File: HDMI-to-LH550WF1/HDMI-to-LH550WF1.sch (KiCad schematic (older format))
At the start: 2 parts

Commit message: Annotated schematic and associated footprints
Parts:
- P1: renamed from P?; footprint (none) -> Connect:USB_Mini-B
- P2: renamed from P?; footprint (none) -> connectors:FCI_10029449-111RLF
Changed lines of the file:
@@
 $EndSheet
 $Comp
-L USB_OTG P?
+L USB_OTG P1
 U 1 1 583A5572
 P 2300 4500
-F 0 "P?" H 2625 4375 50  0000 C CNN
+F 0 "P1" H 2625 4375 50  0000 C CNN
 F 1 "USB_OTG" H 2300 4700 50  0000 C CNN
-F 2 "" V 2250 4400 50  0000 C CNN
+F 2 "Connect:USB_Mini-B" V 2250 4400 50  0001 C CNN
 F 3 "" V 2250 4400 50  0000 C CNN
 	1    2300 4500
@@
 NoConn ~ 2600 4400
 $Comp
-L GND #PWR?
+L GND #PWR01
 U 1 1 583A6AC9
 P 1900 4200
-F 0 "#PWR?" H 1900 3950 50  0001 C CNN
+F 0 "#PWR01" H 1900 3950 50  0001 C CNN
 F 1 "GND" H 1900 4050 50  0000 C CNN
 F 2 "" H 1900 4200 50  0000 C CNN
@@
 	3100 4700 2600 4700
 $Comp
-L GND #PWR?
+L GND #PWR02
 U 1 1 58414197
 P 3300 1400
-F 0 "#PWR?" H 3300 1150 50  0001 C CNN
+F 0 "#PWR02" H 3300 1150 50  0001 C CNN
 F 1 "GND" H 3300 1250 50  0000 C CNN
 F 2 "" H 3300 1400 50  0000 C CNN
@@
 HPD
 $Comp
-L GND #PWR?
+L GND #PWR03
 U 1 1 5841821A
 P 3600 1700
-F 0 "#PWR?" H 3600 1450 50  0001 C CNN
+F 0 "#PWR03" H 3600 1450 50  0001 C CNN
 F 1 "GND" H 3600 1550 50  0000 C CNN
 F 2 "" H 3600 1700 50  0000 C CNN
@@
 $EndComp
 $Comp
-L GND #PWR?
+L GND #PWR04
 U 1 1 5841833B
 P 3600 2000
-F 0 "#PWR?" H 3600 1750 50  0001 C CNN
+F 0 "#PWR04" H 3600 1750 50  0001 C CNN
 F 1 "GND" H 3600 1850 50  0000 C CNN
 F 2 "" H 3600 2000 50  0000 C CNN
@@
 $EndComp
 $Comp
-L GND #PWR?
+L GND #PWR05
 U 1 1 5841845A
 P 3600 2300
-F 0 "#PWR?" H 3600 2050 50  0001 C CNN
+F 0 "#PWR05" H 3600 2050 50  0001 C CNN
 F 1 "GND" H 3600 2150 50  0000 C CNN
 F 2 "" H 3600 2300 50  0000 C CNN
@@
 $EndComp
 $Comp
-L GND #PWR?
+L GND #PWR06
 U 1 1 58418579
 P 3600 2600
-F 0 "#PWR?" H 3600 2350 50  0001 C CNN
+F 0 "#PWR06" H 3600 2350 50  0001 C CNN
 F 1 "GND" H 3600 2450 50  0000 C CNN
 F 2 "" H 3600 2600 50  0000 C CNN
@@
 $EndComp
 $Comp
-L GND #PWR?
+L GND #PWR07
 U 1 1 58418698
 P 3600 3200
-F 0 "#PWR?" H 3600 2950 50  0001 C CNN
+F 0 "#PWR07" H 3600 2950 50  0001 C CNN
 F 1 "GND" H 3600 3050 50  0000 C CNN
 F 2 "" H 3600 3200 50  0000 C CNN
@@
 CLKP
 $Comp
-L HDMI P?
+L HDMI P2
 U 1 1 584141D8
 P 2800 2400
-F 0 "P?" H 2600 3650 60  0000 L CNN
+F 0 "P2" H 2600 3650 60  0000 L CNN
 F 1 "HDMI" H 2600 1150 60  0000 L CNN
-F 2 "" H 2700 2300 60  0001 C CNN
+F 2 "connectors:FCI_10029449-111RLF" H 2700 2300 60  0001 C CNN
 F 3 "" H 2700 2300 60  0001 C CNN
 	1    2800 2400

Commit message: Renamed some nets to enable differential routing
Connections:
- net labels added: CLK_N, CLK_P, D0_N, D0_P, D1_N, D1_P, D2_N, D2_P
- net labels removed: CLKN, CLKP, D0N, D0P, D1N, D1P, D2N, D2P
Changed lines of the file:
@@
 F0 "LCD-Panel" 60
 F1 "LCD-Panel.sch" 60
-F2 "DATA3P" I L 8500 2900 60
-F3 "DATA3N" I L 8500 2800 60
-F4 "DATA2P" I L 8500 3100 60
-F5 "DATA2N" I L 8500 3000 60
-F6 "CLKP" I L 8500 3700 60
-F7 "CLKN" I L 8500 3600 60
-F8 "DATA1N" I L 8500 3200 60
-F9 "DATA1P" I L 8500 3300 60
-F10 "DATA0P" I L 8500 3500 60
-F11 "DATA0N" I L 8500 3400 60
+F2 "DATA3_P" I L 8500 2900 60
+F3 "DATA3_N" I L 8500 2800 60
+F4 "DATA2_P" I L 8500 3100 60
+F5 "DATA2_N" I L 8500 3000 60
+F6 "CLK_P" I L 8500 3700 60
+F7 "CLK_N" I L 8500 3600 60
+F8 "DATA1_N" I L 8500 3200 60
+F9 "DATA1_P" I L 8500 3300 60
+F10 "DATA0_P" I L 8500 3500 60
+F11 "DATA0_N" I L 8500 3400 60
 F12 "RESET" I L 8500 3900 60
 $EndSheet
@@
 	3200 1600 3600 1600
 Text Label 3600 1600 2    60   ~ 0
-D2P
+D2_P
 Text Label 3600 1800 2    60   ~ 0
-D2N
+D2_N
 Text Label 3600 1900 2    60   ~ 0
-D1P
+D1_P
 Text Label 3600 2100 2    60   ~ 0
-D1N
+D1_N
 Text Label 3600 2200 2    60   ~ 0
-D0P
+D0_P
 Text Label 3600 2400 2    60   ~ 0
-D0N
+D0_N
 Text Label 3600 2500 2    60   ~ 0
-CLKP
+CLK_P
 Text Label 3600 2700 2    60   ~ 0
-CLKN
+CLK_N
 Text Label 3600 3000 2    60   ~ 0
 SCL
@@
 SCL
 Text Label 5300 3500 0    60   ~ 0
-D2N
+D2_N
 Text Label 5300 3400 0    60   ~ 0
-D2P
+D2_P
 Text Label 5300 3300 0    60   ~ 0
-D1N
+D1_N
 Text Label 5300 3200 0    60   ~ 0
-D1P
+D1_P
 Text Label 5300 3100 0    60   ~ 0
-D0N
+D0_N
 Text Label 5300 3000 0    60   ~ 0
-D0P
+D0_P
 Text Label 5300 2900 0    60   ~ 0
-CLKN
+CLK_N
 Text Label 5300 2800 0    60   ~ 0
-CLKP
+CLK_P
 $Comp
 L HDMI P2

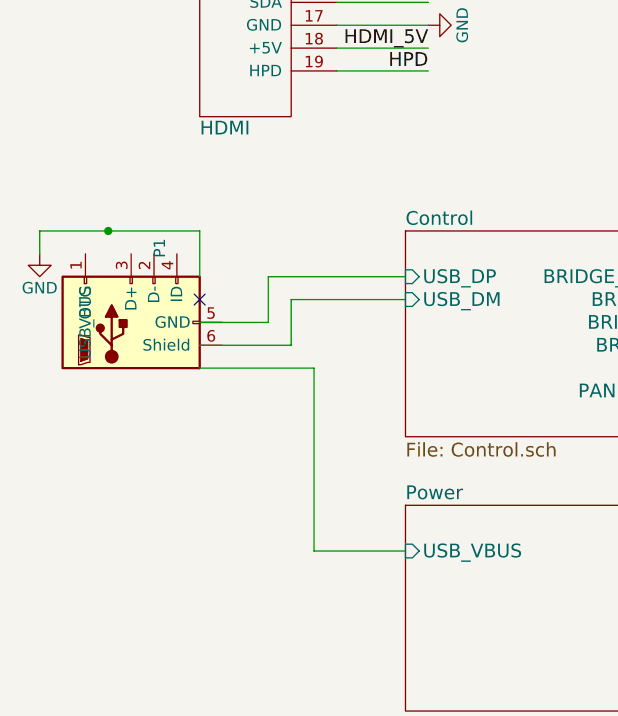
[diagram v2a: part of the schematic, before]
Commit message: Replace USB connector symbol with updated version
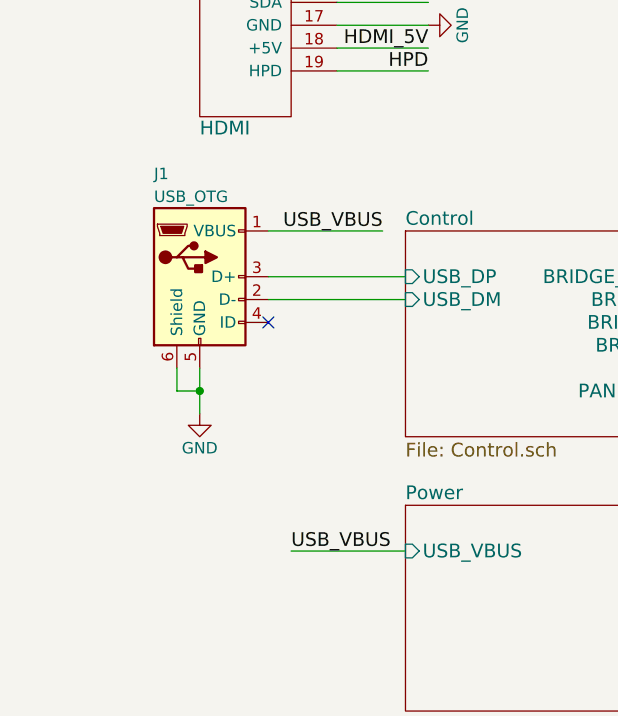
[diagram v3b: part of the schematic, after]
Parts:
- removed P1: USB_OTG, Connect:USB_Mini-B, symbol USB_OTG
- added J1: USB_OTG, Connect:USB_Micro-B, symbol USB_OTG
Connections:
- net labels added: USB_VBUS
- wire segments 67 -> 62
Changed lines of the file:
@@
 $EndSheet
-$Comp
-L USB_OTG P1
-U 1 1 583A5572
-P 2300 4500
-F 0 "P1" H 2625 4375 50  0000 C CNN
-F 1 "USB_OTG" H 2300 4700 50  0000 C CNN
-F 2 "Connect:USB_Mini-B" V 2250 4400 50  0001 C CNN
-F 3 "" V 2250 4400 50  0000 C CNN
-	1    2300 4500
-	0    -1   -1   0
-$EndComp
-NoConn ~ 2600 4400
 $Comp
 L GND #PWR01
 U 1 1 583A6AC9
-P 1900 4200
-F 0 "#PWR01" H 1900 3950 50  0001 C CNN
-F 1 "GND" H 1900 4050 50  0000 C CNN
-F 2 "" H 1900 4200 50  0000 C CNN
-F 3 "" H 1900 4200 50  0000 C CNN
-	1    1900 4200
+P 2600 4900
+F 0 "#PWR01" H 2600 4650 50  0001 C CNN
+F 1 "GND" H 2600 4750 50  0000 C CNN
+F 2 "" H 2600 4900 50  0000 C CNN
+F 3 "" H 2600 4900 50  0000 C CNN
+	1    2600 4900
 	1    0    0    -1
 $EndComp
@@
 	7300 3700 8500 3700
 Wire Wire Line
-	2600 4100 2600 4300
-Wire Wire Line
-	1900 4100 2600 4100
-Wire Wire Line
-	1900 4100 1900 4200
-Connection ~ 2200 4100
+	2600 4700 2600 4900
 Wire Wire Line
 	5200 4100 5200 4300
@@
 	7600 3900 8500 3900
 Wire Wire Line
-	2600 4500 2900 4500
-Wire Wire Line
-	2600 4600 3000 4600
-Wire Wire Line
 	5200 4300 4900 4300
 Wire Wire Line
@@
 	3500 4300 2900 4300
 Wire Wire Line
-	2900 4300 2900 4500
-Wire Wire Line
-	3500 4400 3000 4400
-Wire Wire Line
-	3000 4400 3000 4600
-Wire Wire Line
-	3500 5500 3100 5500
-Wire Wire Line
-	3100 5500 3100 4700
-Wire Wire Line
-	3100 4700 2600 4700
+	2900 4400 3500 4400
+Wire Wire Line
+	3000 5500 3500 5500
 $Comp
 L GND #PWR02
@@
 	1    0    0    -1
 $EndComp
+$Comp
+L USB_OTG J1
+U 1 1 58F8583B
+P 2600 4300
+F 0 "J1" H 2400 4750 50  0000 L CNN
+F 1 "USB_OTG" H 2400 4650 50  0000 L CNN
+F 2 "Connect:USB_Micro-B" H 2750 4250 50  0001 C CNN
+F 3 "" H 2750 4250 50  0001 C CNN
+	1    2600 4300
+	1    0    0    -1
+$EndComp
+Wire Wire Line
+	2500 4700 2500 4800
+Wire Wire Line
+	2500 4800 2600 4800
+Connection ~ 2600 4800
+Text Label 3400 4100 2    60   ~ 0
+USB_VBUS
+Wire Wire Line
+	3400 4100 2900 4100
+NoConn ~ 2900 4500
+Text Label 3000 5500 0    60   ~ 0
+USB_VBUS
 $EndSCHEMATC
